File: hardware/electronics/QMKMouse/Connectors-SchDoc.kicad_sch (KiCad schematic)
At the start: 19 parts

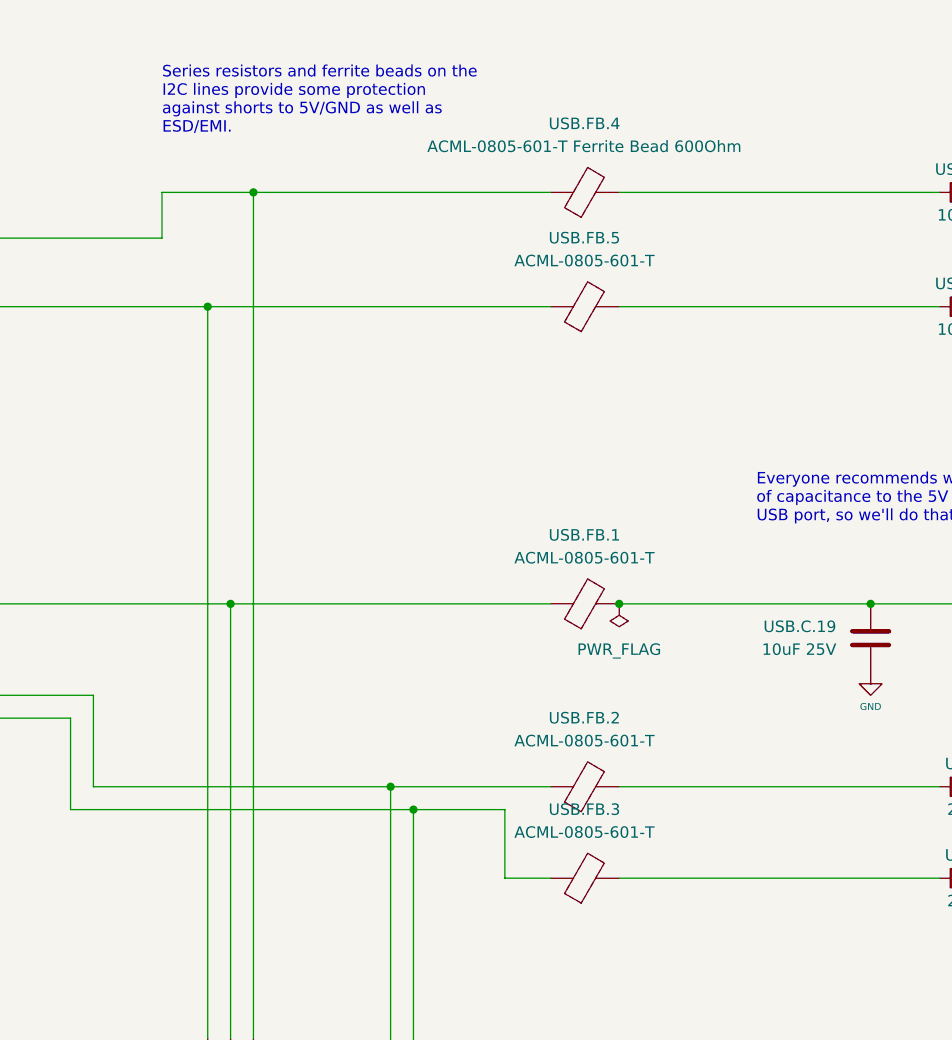
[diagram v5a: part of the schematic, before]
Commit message: fix minor Schematic naming errors; improve BoM generation
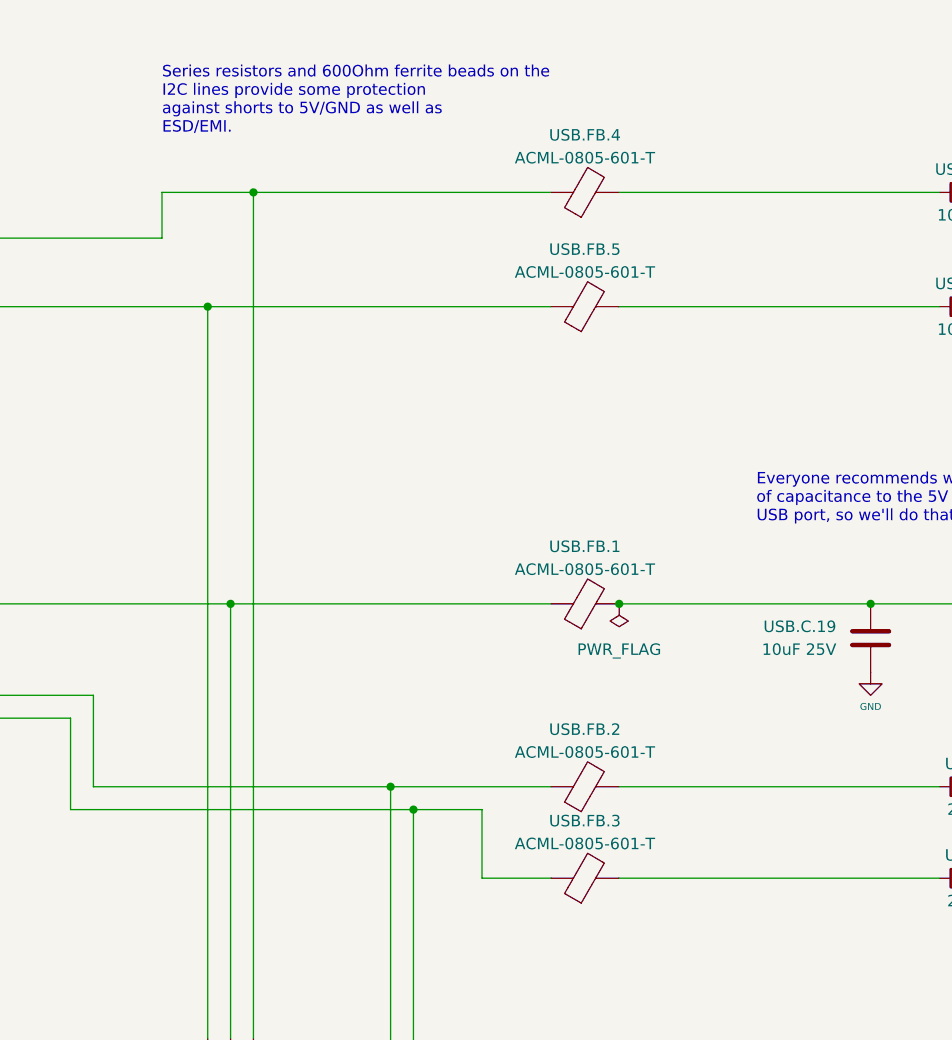
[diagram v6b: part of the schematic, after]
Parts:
- USB.FB.4: value ACML-0805-601-T Ferrite Bead 600Ohm -> ACML-0805-601-T
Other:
- note added: "Series resistors and 600Ohm ferrite beads on the I2C lines provide some protection against shorts to 5V/GND as well as ESD/EMI."
- note removed: "Series resistors and ferrite beads on the I2C lines provide some protection against shorts to 5V/GND as well as ESD/EMI."
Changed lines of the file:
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@@
     (stroke (width 0) (type default) (color 0 0 0 0))
   )
-  (wire (pts (xy 182.88 120.65) (xy 177.8 120.65))
+  (wire (pts (xy 182.88 120.65) (xy 175.26 120.65))
     (stroke (width 0) (type default) (color 0 0 0 0))
   )
@@
     (stroke (width 0) (type default) (color 0 0 0 0))
   )
-  (wire (pts (xy 177.8 113.03) (xy 167.64 113.03))
+  (wire (pts (xy 175.26 113.03) (xy 167.64 113.03))
     (stroke (width 0) (type default) (color 0 0 0 0))
   )
@@
     (stroke (width 0) (type default) (color 0 0 0 0))
   )
-  (wire (pts (xy 177.8 120.65) (xy 177.8 113.03))
+  (wire (pts (xy 175.26 120.65) (xy 175.26 113.03))
     (stroke (width 0) (type default) (color 0 0 0 0))
   )
@@
     (effects (font (size 1.27 1.27)) (justify left bottom))
   )
-  (text "Series resistors and ferrite beads on the\nI2C lines provide some protection \nagainst shorts to 5V/GND as well as \nESD/EMI."
+  (text "Series resistors and 600Ohm ferrite beads on the\nI2C lines provide some protection \nagainst shorts to 5V/GND as well as \nESD/EMI."
     (at 139.7 38.1 0)
     (effects (font (size 1.27 1.27)) (justify left bottom))
@@
     (pin "1")
   )
-  (symbol (lib_name "FerriteBead_1") (lib_id "Device:FerriteBead") (at 186.69 90.17 90) (unit 1)
-    (in_bom yes) (on_board yes) (fields_autoplaced)
-    (property "Reference" "USB.FB.1" (id 0) (at 186.6392 82.55 90))
-    (property "Value" "ACML-0805-601-T" (id 1) (at 186.6392 85.09 90))
+  (symbol (lib_id "Device:FerriteBead") (at 186.69 90.17 90) (unit 1)
+    (in_bom yes) (on_board yes)
+    (property "Reference" "USB.FB.1" (id 0) (at 186.69 83.82 90))
+    (property "Value" "ACML-0805-601-T" (id 1) (at 186.69 86.36 90))
     (property "Footprint" "Chip_Passives.PcbLib:0805" (id 2) (at 186.69 91.948 90)
       (effects (font (size 1.27 1.27)) hide)
@@
   )
   (symbol (lib_id "Device:FerriteBead") (at 186.69 57.15 90) (unit 1)
-    (in_bom yes) (on_board yes) (fields_autoplaced)
-    (property "Reference" "USB.FB.5" (id 0) (at 186.6392 49.53 90))
-    (property "Value" "ACML-0805-601-T" (id 1) (at 186.6392 52.07 90))
+    (in_bom yes) (on_board yes)
+    (property "Reference" "USB.FB.5" (id 0) (at 186.69 50.8 90))
+    (property "Value" "ACML-0805-601-T" (id 1) (at 186.69 53.34 90))
     (property "Footprint" "Chip_Passives.PcbLib:0805" (id 2) (at 186.69 58.928 90)
       (effects (font (size 1.27 1.27)) hide)
@@
   )
   (symbol (lib_id "Device:FerriteBead") (at 186.69 110.49 90) (unit 1)
-    (in_bom yes) (on_board yes) (fields_autoplaced)
-    (property "Reference" "USB.FB.2" (id 0) (at 186.6392 102.87 90))
-    (property "Value" "ACML-0805-601-T" (id 1) (at 186.6392 105.41 90))
+    (in_bom yes) (on_board yes)
+    (property "Reference" "USB.FB.2" (id 0) (at 186.69 104.14 90))
+    (property "Value" "ACML-0805-601-T" (id 1) (at 186.69 106.68 90))
     (property "Footprint" "Chip_Passives.PcbLib:0805" (id 2) (at 186.69 112.268 90)
       (effects (font (size 1.27 1.27)) hide)
@@
   )
   (symbol (lib_id "Device:FerriteBead") (at 186.69 44.45 90) (unit 1)
-    (in_bom yes) (on_board yes) (fields_autoplaced)
-    (property "Reference" "USB.FB.4" (id 0) (at 186.6392 36.83 90))
-    (property "Value" "ACML-0805-601-T Ferrite Bead 600Ohm" (id 1) (at 186.6392 39.37 90))
+    (in_bom yes) (on_board yes)
+    (property "Reference" "USB.FB.4" (id 0) (at 186.69 38.1 90))
+    (property "Value" "ACML-0805-601-T" (id 1) (at 186.69 40.64 90))
     (property "Footprint" "Chip_Passives.PcbLib:0805" (id 2) (at 186.69 46.228 90)
       (effects (font (size 1.27 1.27)) hide)
@@
   )
   (symbol (lib_id "Device:FerriteBead") (at 186.69 120.65 90) (unit 1)
-    (in_bom yes) (on_board yes) (fields_autoplaced)
-    (property "Reference" "USB.FB.3" (id 0) (at 186.6392 113.03 90))
-    (property "Value" "ACML-0805-601-T" (id 1) (at 186.6392 115.57 90))
+    (in_bom yes) (on_board yes)
+    (property "Reference" "USB.FB.3" (id 0) (at 186.69 114.3 90))
+    (property "Value" "ACML-0805-601-T" (id 1) (at 186.69 116.84 90))
     (property "Footprint" "Chip_Passives.PcbLib:0805" (id 2) (at 186.69 122.428 90)
       (effects (font (size 1.27 1.27)) hide)

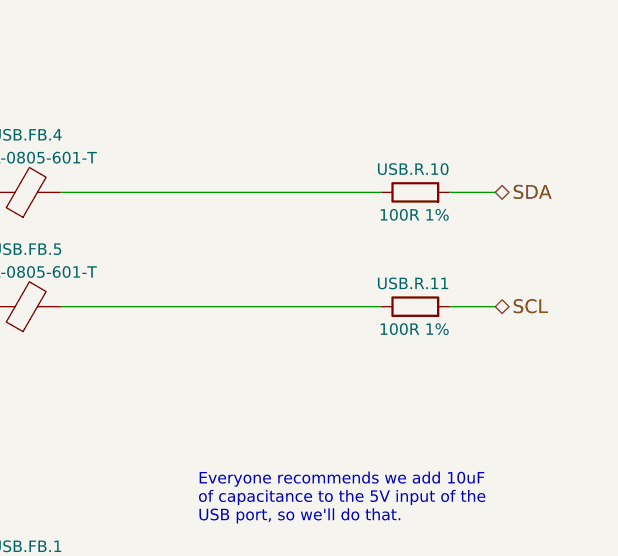
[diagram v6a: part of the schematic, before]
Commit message: correct 2 resistor values and further improve BoM (BoM matches Altium BoM now)
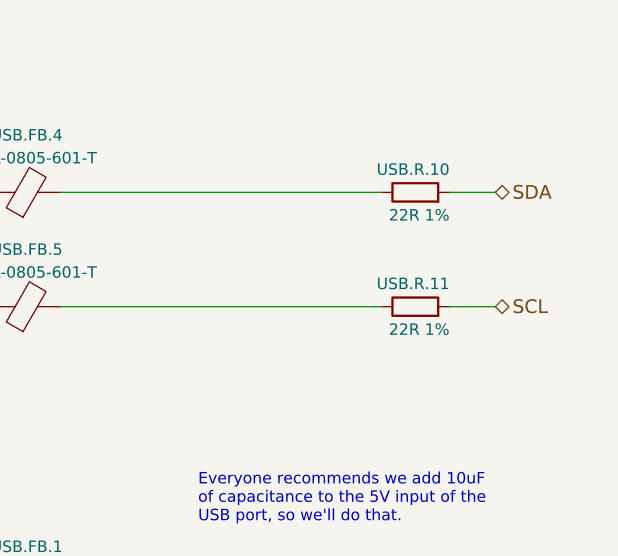
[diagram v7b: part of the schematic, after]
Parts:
- USB.R.10, USB.R.11: value 100R 1% -> 22R 1%
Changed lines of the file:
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@@
       (effects (font (size 1.27 1.27)) (justify left))
     )
-    (property "Value" "100R 1%" (id 1) (at 233.68 59.69 90)
+    (property "Value" "22R 1%" (id 1) (at 233.68 59.69 90)
       (effects (font (size 1.27 1.27)) (justify left))
     )
@@
       (effects (font (size 1.27 1.27)) (justify left))
     )
-    (property "Value" "100R 1%" (id 1) (at 233.68 46.99 90)
-      (effects (font (size 1.27 1.27)) (justify left))
-    )
+    (property "Value" "22R 1%" (id 1) (at 233.68 46.99 90)
+      (effects (font (size 1.27 1.27)) (justify left))
+    )

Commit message: reference 3d model to all components
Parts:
- USB.C.19: footprint Chip_Passives.PcbLib:0805 -> mouse_part:C_0805
- USB.FB.1, USB.FB.2, USB.FB.3, USB.FB.4, USB.FB.5, USB.R.10, USB.R.11, USB.R.12, USB.R.13, USB.R.14, USB.R.15, USB.R.6, USB.R.7, USB.R.8, USB.R.9: footprint Chip_Passives.PcbLib:0805 -> mouse_part:0805
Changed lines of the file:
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@@
     (property "Reference" "USB.FB.1" (id 0) (at 186.69 83.82 90))
     (property "Value" "ACML-0805-601-T" (id 1) (at 186.69 86.36 90))
-    (property "Footprint" "Chip_Passives.PcbLib:0805" (id 2) (at 186.69 91.948 90)
+    (property "Footprint" "mouse_part:0805" (id 2) (at 186.69 91.948 90)
       (effects (font (size 1.27 1.27)) hide)
     )
@@
     (property "Reference" "USB.FB.5" (id 0) (at 186.69 50.8 90))
     (property "Value" "ACML-0805-601-T" (id 1) (at 186.69 53.34 90))
-    (property "Footprint" "Chip_Passives.PcbLib:0805" (id 2) (at 186.69 58.928 90)
+    (property "Footprint" "mouse_part:0805" (id 2) (at 186.69 58.928 90)
       (effects (font (size 1.27 1.27)) hide)
     )
@@
       (effects (font (size 1.27 1.27)) (justify left))
     )
-    (property "Footprint" "Chip_Passives.PcbLib:0805" (id 2) (at 85.598 35.56 90)
+    (property "Footprint" "mouse_part:0805" (id 2) (at 85.598 35.56 90)
       (effects (font (size 1.27 1.27)) hide)
     )
@@
       (effects (font (size 1.27 1.27)) (justify left))
     )
-    (property "Footprint" "Chip_Passives.PcbLib:0805" (id 2) (at 229.87 58.928 90)
+    (property "Footprint" "mouse_part:0805" (id 2) (at 229.87 58.928 90)
       (effects (font (size 1.27 1.27)) hide)
     )
@@
       (effects (font (size 1.27 1.27)) (justify left))
     )
-    (property "Footprint" "Chip_Passives.PcbLib:0805" (id 2) (at 67.818 120.65 90)
+    (property "Footprint" "mouse_part:0805" (id 2) (at 67.818 120.65 90)
       (effects (font (size 1.27 1.27)) hide)
     )
@@
       (effects (font (size 1.27 1.27)) (justify left))
     )
-    (property "Footprint" "Chip_Passives.PcbLib:0805" (id 2) (at 95.758 120.65 90)
+    (property "Footprint" "mouse_part:0805" (id 2) (at 95.758 120.65 90)
       (effects (font (size 1.27 1.27)) hide)
     )
@@
       (effects (font (size 1.27 1.27)) (justify left))
     )
-    (property "Footprint" "Chip_Passives.PcbLib:0805" (id 2) (at 103.378 35.56 90)
+    (property "Footprint" "mouse_part:0805" (id 2) (at 103.378 35.56 90)
       (effects (font (size 1.27 1.27)) hide)
     )
@@
     (property "Reference" "USB.FB.2" (id 0) (at 186.69 104.14 90))
     (property "Value" "ACML-0805-601-T" (id 1) (at 186.69 106.68 90))
-    (property "Footprint" "Chip_Passives.PcbLib:0805" (id 2) (at 186.69 112.268 90)
+    (property "Footprint" "mouse_part:0805" (id 2) (at 186.69 112.268 90)
       (effects (font (size 1.27 1.27)) hide)
     )
@@
       (effects (font (size 1.27 1.27)) (justify left))
     )
-    (property "Footprint" "Chip_Passives.PcbLib:0805" (id 2) (at 105.918 120.65 90)
+    (property "Footprint" "mouse_part:0805" (id 2) (at 105.918 120.65 90)
       (effects (font (size 1.27 1.27)) hide)
     )
@@
       (effects (font (size 1.27 1.27)) (justify right))
     )
-    (property "Footprint" "Chip_Passives.PcbLib:0805" (id 2) (at 219.4052 90.17 0)
+    (property "Footprint" "mouse_part:C_0805" (id 2) (at 219.4052 90.17 0)
       (effects (font (size 1.27 1.27)) hide)
     )
@@
     (property "Reference" "USB.FB.4" (id 0) (at 186.69 38.1 90))
     (property "Value" "ACML-0805-601-T" (id 1) (at 186.69 40.64 90))
-    (property "Footprint" "Chip_Passives.PcbLib:0805" (id 2) (at 186.69 46.228 90)
+    (property "Footprint" "mouse_part:0805" (id 2) (at 186.69 46.228 90)
       (effects (font (size 1.27 1.27)) hide)
     )
@@
     (property "Reference" "USB.FB.3" (id 0) (at 186.69 114.3 90))
     (property "Value" "ACML-0805-601-T" (id 1) (at 186.69 116.84 90))
-    (property "Footprint" "Chip_Passives.PcbLib:0805" (id 2) (at 186.69 122.428 90)
+    (property "Footprint" "mouse_part:0805" (id 2) (at 186.69 122.428 90)
       (effects (font (size 1.27 1.27)) hide)
     )
@@
       (effects (font (size 1.27 1.27)) (justify left))
     )
-    (property "Footprint" "Chip_Passives.PcbLib:0805" (id 2) (at 229.87 112.268 90)
+    (property "Footprint" "mouse_part:0805" (id 2) (at 229.87 112.268 90)
       (effects (font (size 1.27 1.27)) hide)
     )
@@
       (effects (font (size 1.27 1.27)) (justify left))
     )
-    (property "Footprint" "Chip_Passives.PcbLib:0805" (id 2) (at 77.978 120.65 90)
+    (property "Footprint" "mouse_part:0805" (id 2) (at 77.978 120.65 90)
       (effects (font (size 1.27 1.27)) hide)
     )
@@
       (effects (font (size 1.27 1.27)) (justify left))
     )
-    (property "Footprint" "Chip_Passives.PcbLib:0805" (id 2) (at 229.87 122.428 90)
+    (property "Footprint" "mouse_part:0805" (id 2) (at 229.87 122.428 90)
       (effects (font (size 1.27 1.27)) hide)
     )
@@
       (effects (font (size 1.27 1.27)) (justify left))
     )
-    (property "Footprint" "Chip_Passives.PcbLib:0805" (id 2) (at 229.87 46.228 90)
-      (effects (font (size 1.27 1.27)) hide)
-    )
+    (property "Footprint" "mouse_part:0805" (id 2) (at 229.87 46.228 90)
+      (effects (font (size 1.27 1.27)) hide)
+    )
